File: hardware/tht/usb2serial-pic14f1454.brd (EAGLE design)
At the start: 46.4 x 28 mm, 14 parts, among them IC1 PIC16F1454, IC2 LP2950-33, J1 USB-SHIELD-A-H, J2 J2

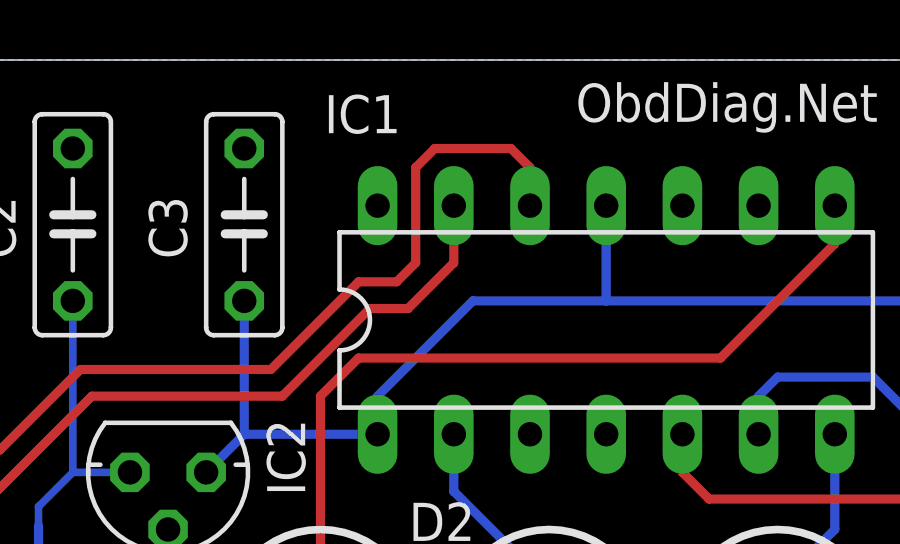
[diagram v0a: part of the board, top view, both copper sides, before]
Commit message: Fixed D+/D- bug
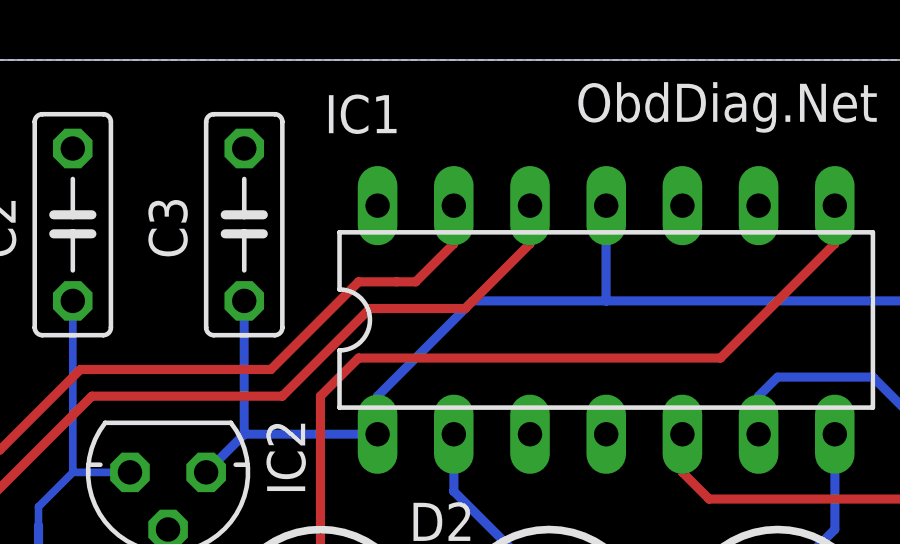
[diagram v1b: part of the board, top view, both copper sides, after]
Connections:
- net N$1: now also IC1.12; no longer IC1.13
- net N$2: now also IC1.13; no longer IC1.12
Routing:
- net N$2: track 27.4 -> 21.4 mm
- net N$1: track 22.6 -> 24.8 mm
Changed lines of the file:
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@@
 <signal name="N$1">
 <contactref element="J1" pad="D-"/>
-<contactref element="IC1" pad="13"/>
 <wire x1="4.9" y1="7" x2="6.365" y2="7" width="0.3048" layer="1"/>
 <wire x1="6.365" y1="7" x2="10.16" y2="10.795" width="0.3048" layer="1"/>
 <wire x1="10.16" y1="10.795" x2="16.51" y2="10.795" width="0.3048" layer="1"/>
 <wire x1="16.51" y1="10.795" x2="19.431" y2="13.716" width="0.3048" layer="1"/>
-<wire x1="19.431" y1="13.716" x2="20.701" y2="13.716" width="0.3048" layer="1"/>
-<wire x1="20.701" y1="13.716" x2="22.225" y2="15.24" width="0.3048" layer="1"/>
-<wire x1="22.225" y1="15.24" x2="22.225" y2="17.145" width="0.3048" layer="1"/>
+<contactref element="IC1" pad="12"/>
+<wire x1="24.765" y1="17.145" x2="24.765" y2="15.875" width="0.3048" layer="1"/>
+<wire x1="19.431" y1="13.716" x2="22.606" y2="13.716" width="0.3048" layer="1"/>
+<wire x1="22.606" y1="13.716" x2="24.765" y2="15.875" width="0.3048" layer="1"/>
 </signal>
 <signal name="N$2">
 <contactref element="J1" pad="D+"/>
-<contactref element="IC1" pad="12"/>
 <wire x1="4.9" y1="9" x2="7.095" y2="9" width="0.3048" layer="1"/>
 <wire x1="9.779" y1="11.684" x2="16.129" y2="11.684" width="0.3048" layer="1"/>
 <wire x1="16.129" y1="11.684" x2="19.05" y2="14.605" width="0.3048" layer="1"/>
 <wire x1="19.05" y1="14.605" x2="20.32" y2="14.605" width="0.3048" layer="1"/>
-<wire x1="20.32" y1="14.605" x2="20.955" y2="15.24" width="0.3048" layer="1"/>
-<wire x1="20.955" y1="15.24" x2="20.955" y2="18.415" width="0.3048" layer="1"/>
-<wire x1="21.59" y1="19.05" x2="24.13" y2="19.05" width="0.3048" layer="1"/>
-<wire x1="24.13" y1="19.05" x2="24.765" y2="18.415" width="0.3048" layer="1"/>
-<wire x1="24.765" y1="18.415" x2="24.765" y2="17.145" width="0.3048" layer="1"/>
-<wire x1="20.955" y1="18.415" x2="21.59" y2="19.05" width="0.3048" layer="1"/>
 <wire x1="9.779" y1="11.684" x2="7.095" y2="9" width="0.3048" layer="1"/>
+<contactref element="IC1" pad="13"/>
+<wire x1="22.225" y1="17.145" x2="22.225" y2="15.875" width="0.3048" layer="1"/>
+<wire x1="20.32" y1="14.605" x2="20.955" y2="14.605" width="0.3048" layer="1"/>
+<wire x1="20.955" y1="14.605" x2="22.225" y2="15.875" width="0.3048" layer="1"/>
 </signal>
 <signal name="TX">
